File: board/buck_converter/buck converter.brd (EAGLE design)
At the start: 28.3 x 14.5 mm, 8 parts, among them IC1 TPS84621

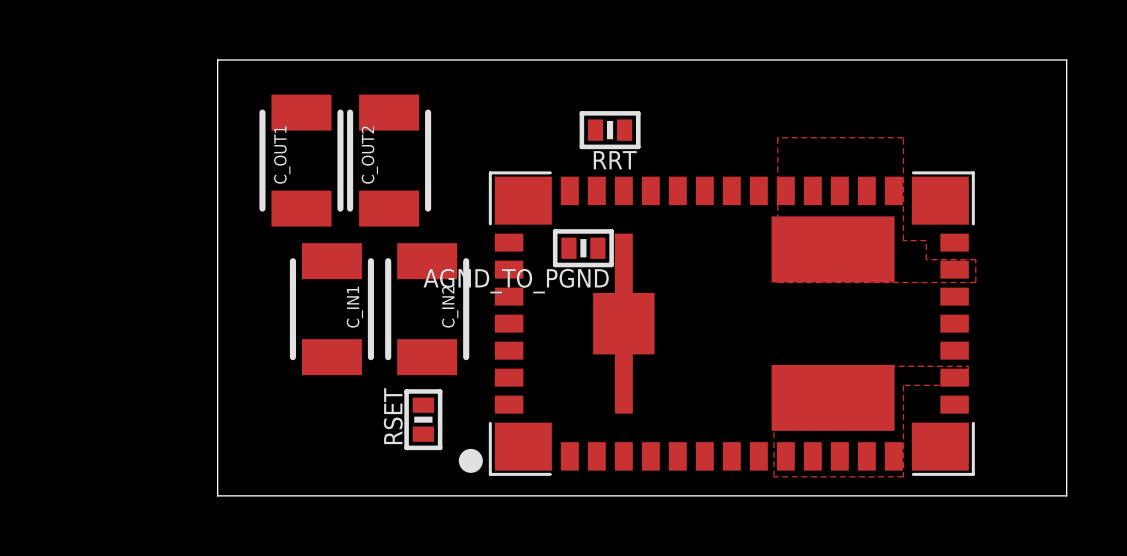
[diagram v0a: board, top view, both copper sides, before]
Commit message: Some routing polygons added.
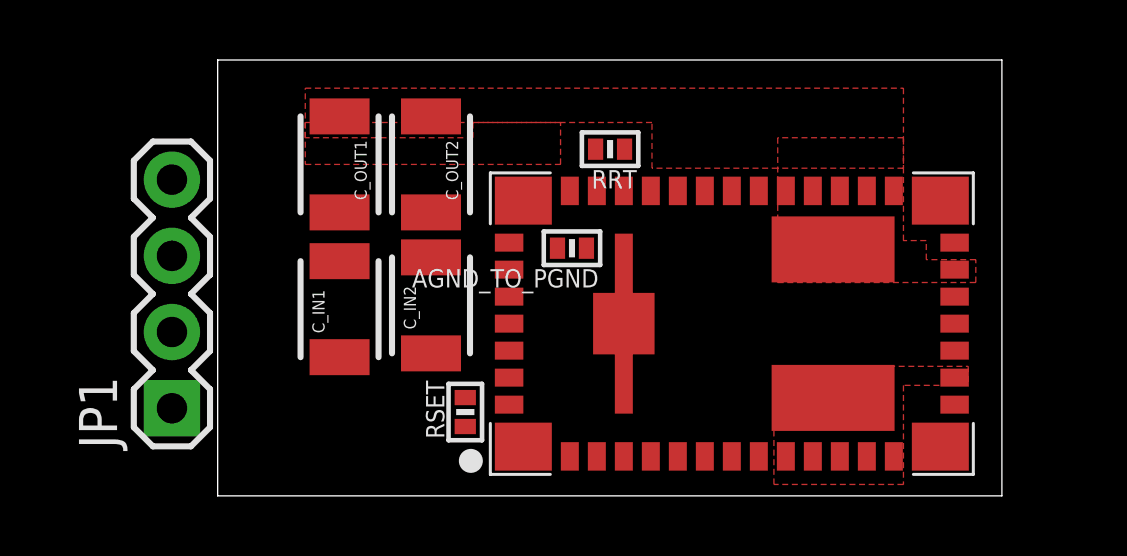
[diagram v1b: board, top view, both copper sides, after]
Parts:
- added JP1: (no value), SparkFun-Connectors:1X04
- moved RSET 1.42 mm to (8.26, 2.79)
- moved C_OUT2 1.40 mm to (7.11, 11.0), turned to 270 degrees
- moved C_OUT1 1.28 mm to (4.06, 11.0), turned to 270 degrees
- moved RRT 0.63 mm to (13.1, 11.6)
- moved AGND_TO_PGND 0.38 mm to (11.8, 8.26)
- moved C_IN1 0.25 mm to (4.06, 6.22), turned to 90 degrees
- moved C_IN2 0.18 mm to (7.11, 6.35), turned to 90 degrees
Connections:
- new net PWRGD: IC1.33, JP1.4
- net GND: now also JP1.2
- net VIN: now also JP1.1
- net VOUT: now also JP1.3
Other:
- board size 28.3 x 14.5 mm -> 26.1 x 14.5 mm
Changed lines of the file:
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@@
 <board>
 <plain>
-<wire x1="0" y1="0" x2="28.301" y2="0" width="0" layer="20"/>
-<wire x1="28.301" y1="0" x2="28.301" y2="14.529" width="0" layer="20"/>
-<wire x1="28.301" y1="14.529" x2="0" y2="14.529" width="0" layer="20"/>
+<wire x1="0" y1="0" x2="26.142" y2="0" width="0" layer="20"/>
+<wire x1="26.142" y1="0" x2="26.142" y2="14.529" width="0" layer="20"/>
+<wire x1="26.142" y1="14.529" x2="0" y2="14.529" width="0" layer="20"/>
 <wire x1="0" y1="14.529" x2="0" y2="0" width="0" layer="20"/>
 </plain>
@@
 <elements>
 <element name="IC1" library="zumy" package="TPS84621" value="TPS84621" x="15.24" y="7.366"/>
-<element name="C_OUT2" library="biomimetic" package="1210" value="" x="5.715" y="11.176" rot="R90"/>
-<element name="C_OUT1" library="biomimetic" package="1210" value="" x="2.794" y="11.176" rot="R90"/>
-<element name="AGND_TO_PGND" library="biomimetic" package="0402-RES" value="0" x="12.192" y="8.255" rot="R180"/>
-<element name="C_IN1" library="biomimetic" package="1210" value="" x="3.81" y="6.223" rot="R270"/>
-<element name="C_IN2" library="biomimetic" package="1210" value="" x="6.985" y="6.223" rot="R270"/>
-<element name="RSET" library="biomimetic" package="0402-RES" value="196" x="6.858" y="2.54" rot="R90"/>
-<element name="RRT" library="biomimetic" package="0402-RES" value="86.6K" x="13.081" y="12.192" rot="R180"/>
+<element name="C_OUT2" library="biomimetic" package="1210" value="" x="7.112" y="11.049" rot="R270"/>
+<element name="C_OUT1" library="biomimetic" package="1210" value="" x="4.064" y="11.049" rot="R270"/>
+<element name="AGND_TO_PGND" library="biomimetic" package="0402-RES" value="0" x="11.811" y="8.255" rot="R180"/>
+<element name="C_IN1" library="biomimetic" package="1210" value="" x="4.064" y="6.223" rot="R90"/>
+<element name="C_IN2" library="biomimetic" package="1210" value="" x="7.112" y="6.35" rot="R90"/>
+<element name="RSET" library="biomimetic" package="0402-RES" value="196" x="8.255" y="2.794" rot="R90"/>
+<element name="RRT" library="biomimetic" package="0402-RES" value="86.6K" x="13.081" y="11.557" rot="R180"/>
+<element name="JP1" library="SparkFun-Connectors" package="1X04" value="" x="-1.524" y="2.921" rot="R90"/>
 </elements>
 <signals>
@@
 <vertex x="22.86" y="11.938"/>
 </polygon>
+<contactref element="JP1" pad="3"/>
+<polygon width="0" layer="1" thermals="no">
+<vertex x="18.669" y="10.922"/>
+<vertex x="14.478" y="10.922"/>
+<vertex x="14.478" y="12.446"/>
+<vertex x="8.509" y="12.446"/>
+<vertex x="8.509" y="11.938"/>
+<vertex x="2.921" y="11.938"/>
+<vertex x="2.921" y="13.589"/>
+<vertex x="22.86" y="13.589"/>
+<vertex x="22.86" y="10.922"/>
+</polygon>
 <wire x1="18.94" y1="10.166" x2="18.04" y2="10.166" width="0" layer="19" extent="1-1"/>
-<wire x1="9.715" y1="3.041" x2="18.04" y2="10.166" width="0" layer="19" extent="1-1"/>
-<wire x1="5.715" y1="9.576" x2="9.715" y2="3.041" width="0" layer="19" extent="1-1"/>
-<wire x1="2.794" y1="9.576" x2="5.715" y2="9.576" width="0" layer="19" extent="1-1"/>
+<wire x1="-1.524" y1="8.001" x2="4.064" y2="12.649" width="0" layer="19" extent="1-1"/>
+<wire x1="9.715" y1="3.041" x2="7.112" y2="12.649" width="0" layer="19" extent="1-1"/>
+<polygon width="0" layer="1" thermals="no">
+<vertex x="2.921" y="12.446"/>
+<vertex x="2.921" y="11.049"/>
+<vertex x="11.43" y="11.049"/>
+<vertex x="11.43" y="12.446"/>
+</polygon>
 </signal>
 <signal name="GND">
@@
 <contactref element="C_IN1" pad="2"/>
 <contactref element="C_IN2" pad="2"/>
+<contactref element="JP1" pad="2"/>
 <wire x1="10.19" y1="9.841" x2="11.74" y2="10.166" width="0" layer="19" extent="1-1"/>
 <wire x1="9.715" y1="8.441" x2="10.19" y2="9.841" width="0" layer="19" extent="1-1"/>
-<wire x1="11.7094" y1="8.255" x2="11.74" y2="10.166" width="0" layer="19" extent="1-1"/>
-<wire x1="6.985" y1="4.623" x2="9.715" y2="8.441" width="0" layer="19" extent="1-1"/>
-<wire x1="3.81" y1="4.623" x2="6.985" y2="4.623" width="0" layer="19" extent="1-1"/>
-<wire x1="5.715" y1="12.776" x2="10.19" y2="9.841" width="0" layer="19" extent="1-1"/>
-<wire x1="2.794" y1="12.776" x2="5.715" y2="12.776" width="0" layer="19" extent="1-1"/>
+<wire x1="11.3284" y1="8.255" x2="9.715" y2="8.441" width="0" layer="19" extent="1-1"/>
+<wire x1="7.112" y1="7.95" x2="9.715" y2="8.441" width="0" layer="19" extent="1-1"/>
+<wire x1="7.112" y1="9.449" x2="7.112" y2="7.95" width="0" layer="19" extent="1-1"/>
+<wire x1="4.064" y1="9.449" x2="7.112" y2="9.449" width="0" layer="19" extent="1-1"/>
+<wire x1="4.064" y1="7.823" x2="4.064" y2="9.449" width="0" layer="19" extent="1-1"/>
+<wire x1="-1.524" y1="5.461" x2="4.064" y2="7.823" width="0" layer="19" extent="1-1"/>
 </signal>
 <signal name="AGND">
@@
 <contactref element="RSET" pad="1"/>
 <contactref element="RRT" pad="1"/>
-<wire x1="13.5636" y1="12.192" x2="13.54" y2="10.166" width="0" layer="19" extent="1-1"/>
-<wire x1="12.6746" y1="8.255" x2="13.54" y2="10.166" width="0" layer="19" extent="1-1"/>
-<wire x1="13.54" y1="5.741" x2="12.6746" y2="8.255" width="0" layer="19" extent="1-1"/>
+<wire x1="13.5636" y1="11.557" x2="13.54" y2="10.166" width="0" layer="19" extent="1-1"/>
+<wire x1="12.2936" y1="8.255" x2="13.54" y2="10.166" width="0" layer="19" extent="1-1"/>
+<wire x1="13.54" y1="5.741" x2="12.2936" y2="8.255" width="0" layer="19" extent="1-1"/>
 <wire x1="11.74" y1="1.316" x2="13.54" y2="5.741" width="0" layer="19" extent="1-1"/>
 <wire x1="10.19" y1="1.641" x2="11.74" y2="1.316" width="0" layer="19" extent="1-1"/>
-<wire x1="6.858" y1="2.0574" x2="10.19" y2="1.641" width="0" layer="19" extent="1-1"/>
+<wire x1="8.255" y1="2.3114" x2="10.19" y2="1.641" width="0" layer="19" extent="1-1"/>
 <wire x1="16.24" y1="1.316" x2="11.74" y2="1.316" width="0" layer="19" extent="1-1"/>
 </signal>
@@
 <contactref element="IC1" pad="43"/>
 <contactref element="RSET" pad="2"/>
-<wire x1="6.858" y1="3.0226" x2="9.715" y2="3.941" width="0" layer="19" extent="1-1"/>
+<wire x1="8.255" y1="3.2766" x2="9.715" y2="3.941" width="0" layer="19" extent="1-1"/>
 </signal>
 <signal name="VIN">
@@
 <contactref element="C_IN1" pad="1"/>
 <contactref element="C_IN2" pad="1"/>
+<contactref element="JP1" pad="1"/>
 <wire x1="9.715" y1="6.641" x2="9.715" y2="7.541" width="0" layer="19" extent="1-1"/>
 <wire x1="9.715" y1="5.741" x2="9.715" y2="6.641" width="0" layer="19" extent="1-1"/>
 <wire x1="9.715" y1="4.841" x2="9.715" y2="5.741" width="0" layer="19" extent="1-1"/>
-<wire x1="6.985" y1="7.823" x2="9.715" y2="7.541" width="0" layer="19" extent="1-1"/>
-<wire x1="3.81" y1="7.823" x2="6.985" y2="7.823" width="0" layer="19" extent="1-1"/>
+<wire x1="7.112" y1="4.75" x2="9.715" y2="4.841" width="0" layer="19" extent="1-1"/>
+<wire x1="4.064" y1="4.623" x2="7.112" y2="4.75" width="0" layer="19" extent="1-1"/>
+<wire x1="-1.524" y1="2.921" x2="4.064" y2="4.623" width="0" layer="19" extent="1-1"/>
 </signal>
 <signal name="N$1">
 <contactref element="IC1" pad="35"/>
 <contactref element="RRT" pad="2"/>
-<wire x1="12.5984" y1="12.192" x2="12.64" y2="10.166" width="0" layer="19" extent="1-1"/>
+<wire x1="12.5984" y1="11.557" x2="12.64" y2="10.166" width="0" layer="19" extent="1-1"/>
 </signal>
 <signal name="PH">
@@
 <vertex x="25.019" y="3.683"/>
 <vertex x="22.86" y="3.683"/>
-<vertex x="22.86" y="0.635"/>
-<vertex x="18.542" y="0.635"/>
+<vertex x="22.86" y="0.381"/>
+<vertex x="18.542" y="0.381"/>
 </polygon>
 <contactref element="IC1" pad="10"/>
@@
 <contactref element="IC1" pad="14"/>
 </signal>
+<signal name="PWRGD">
+<contactref element="IC1" pad="33"/>
+<contactref element="JP1" pad="4"/>
+<wire x1="-1.524" y1="10.541" x2="14.44" y2="10.166" width="0" layer="19" extent="1-1"/>
+</signal>
 </signals>
